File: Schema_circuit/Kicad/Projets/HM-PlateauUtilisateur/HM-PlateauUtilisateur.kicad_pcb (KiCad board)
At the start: 2 copper layers, 1 part, among them U1 MPR121DL

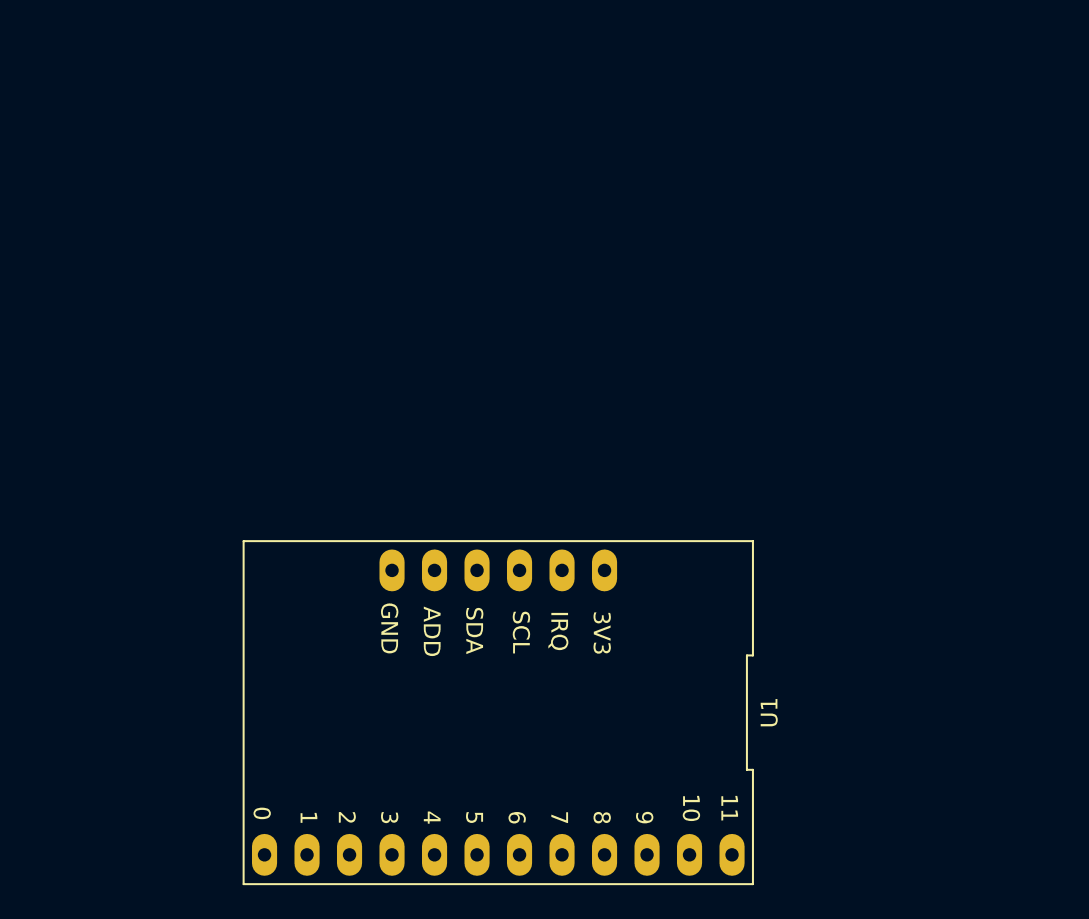
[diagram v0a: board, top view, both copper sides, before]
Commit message: correctif sur PCB PU1
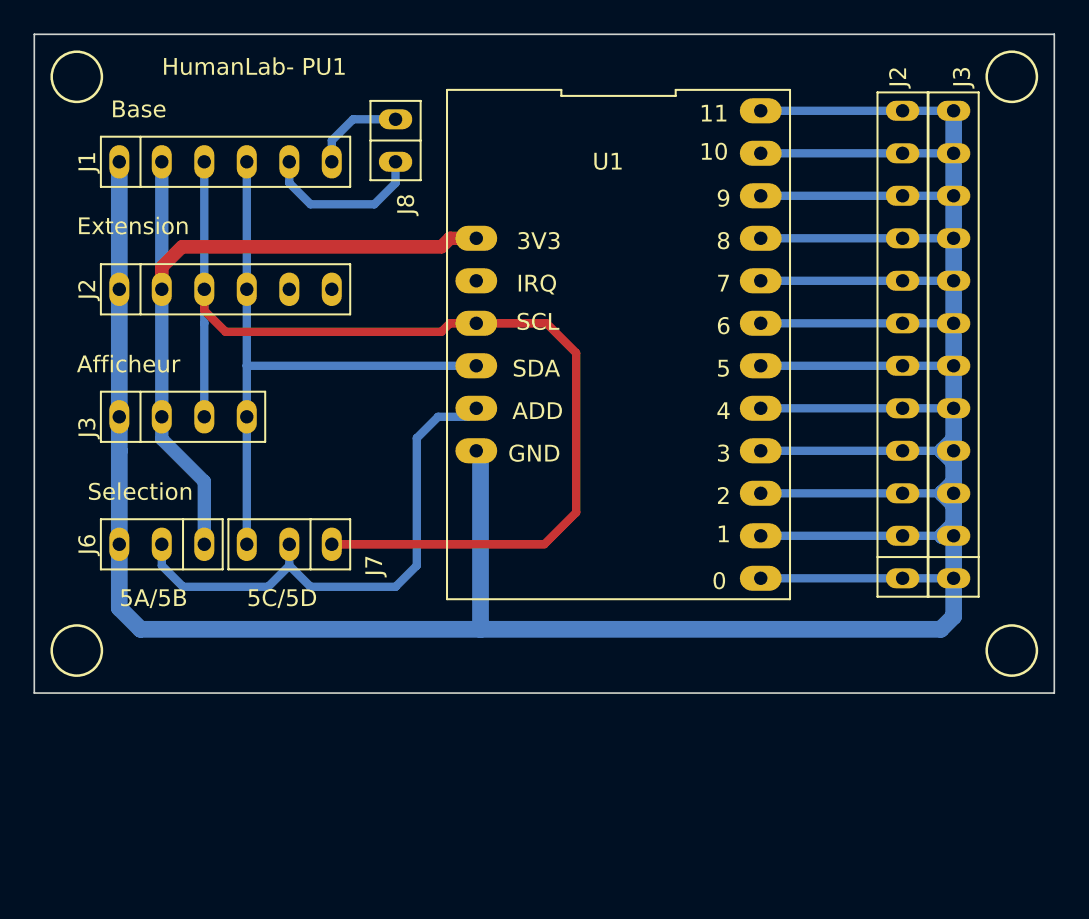
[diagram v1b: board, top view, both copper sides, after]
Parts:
- added J1: Vers Base, MesEmpreintes2:SIP-6, F.Cu at (125.7, 68.6)
- added J2: Exten, MesEmpreintes2:SIP-6, F.Cu at (125.7, 76.2)
- added J2: Conn_01x12_Socket, MesEmpreintes2:SIP-12, F.Cu at (166.2, 79.5)
- added J3: Afficheur, MesEmpreintes2:SIP-4, F.Cu at (123.2, 83.8)
- added J3: Conn_01x12_Socket, MesEmpreintes2:SIP-12, F.Cu at (169.2, 79.5)
- added J6: 5A/5B, MesEmpreintes2:SIP-3, F.Cu at (121.9, 91.4)
- added J7: 5C/5D, MesEmpreintes2:SIP-3, F.Cu at (129.5, 91.4)
- added J8: Conn_01x02_Socket, MesEmpreintes2:SIP-2, F.Cu at (135.9, 67.3)
- moved U1 23.1 mm to (149.2, 79.5), turned to -90 degrees
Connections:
- U1 pad 1: Net-(U1-3V3) -> /3V3
- U1 pad 10: unconnected-(U1-ELE2-Pad10) -> Net-(J2-Pin_4)
- U1 pad 11: unconnected-(U1-ELE3-Pad11) -> Net-(J2-Pin_5)
- U1 pad 12: unconnected-(U1-LED0/ELE4-Pad12) -> Net-(J2-Pin_6)
- U1 pad 13: unconnected-(U1-LED1/ELE5-Pad13) -> Net-(J2-Pin_7)
- U1 pad 14: unconnected-(U1-LED2/ELE6-Pad14) -> Net-(J2-Pin_8)
- U1 pad 15: unconnected-(U1-LED3/ELE7-Pad15) -> Net-(J2-Pin_9)
- U1 pad 16: unconnected-(U1-LED4/ELE8-Pad16) -> Net-(J2-Pin_10)
- U1 pad 18: unconnected-(U1-LED6/ELE10-Pad18) -> Net-(J2-Pin_12)
- U1 pad 3: unconnected-(U1-SCL-Pad3) -> /SCL
- U1 pad 4: Net-(U1-3V3) -> /SDA
- U1 pad 5: unconnected-(U1-ADDR-Pad5) -> Net-(J6-Pin_2)
- U1 pad 6: unconnected-(U1-GND-Pad6) -> /GND
- U1 pad 7: (no net) -> Net-(J2-Pin_1)
- U1 pad 8: unconnected-(U1-ELE0-Pad8) -> Net-(J2-Pin_2)
- U1 pad 9: unconnected-(U1-ELE1-Pad9) -> Net-(J2-Pin_3)
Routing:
- net /GND: track 0.00 -> 130.0 mm
- net /SCL: track 0.00 -> 65.1 mm
- net /3V3: track 0.00 -> 43.4 mm
- net /SDA: track 0.00 -> 36.6 mm
- net Net-(J6-Pin_2): track 0.00 -> 31.8 mm
- net Net-(J2-Pin_9): track 0.00 -> 11.4 mm
- net Net-(J2-Pin_8): track 0.00 -> 11.4 mm
- net Net-(J2-Pin_7): track 0.00 -> 11.4 mm
- net Net-(J2-Pin_6): track 0.00 -> 11.4 mm
- net Net-(J2-Pin_5): track 0.00 -> 11.4 mm
- net Net-(J2-Pin_4): track 0.00 -> 11.4 mm
- net Net-(J2-Pin_3): track 0.00 -> 11.4 mm
- net Net-(J2-Pin_2): track 0.00 -> 11.4 mm
- net Net-(J2-Pin_12): track 0.00 -> 11.4 mm
- net Net-(J2-Pin_11): track 0.00 -> 11.4 mm
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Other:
- board outline added: 61 x 39.4 mm
- board text added: "5A/5B"
- board text added: "5C/5D"
- board text added: "Afficheur"
- board text added: "Base"
- board text added: "Extension"
- board text added: "HumanLab- PU1"
- board text added: "Selection"
